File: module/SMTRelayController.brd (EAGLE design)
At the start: 57.1 x 63.2 mm, 34 parts, among them Q1 2n3904, Q2 2n3904, Q3 2n3904, U1 L298

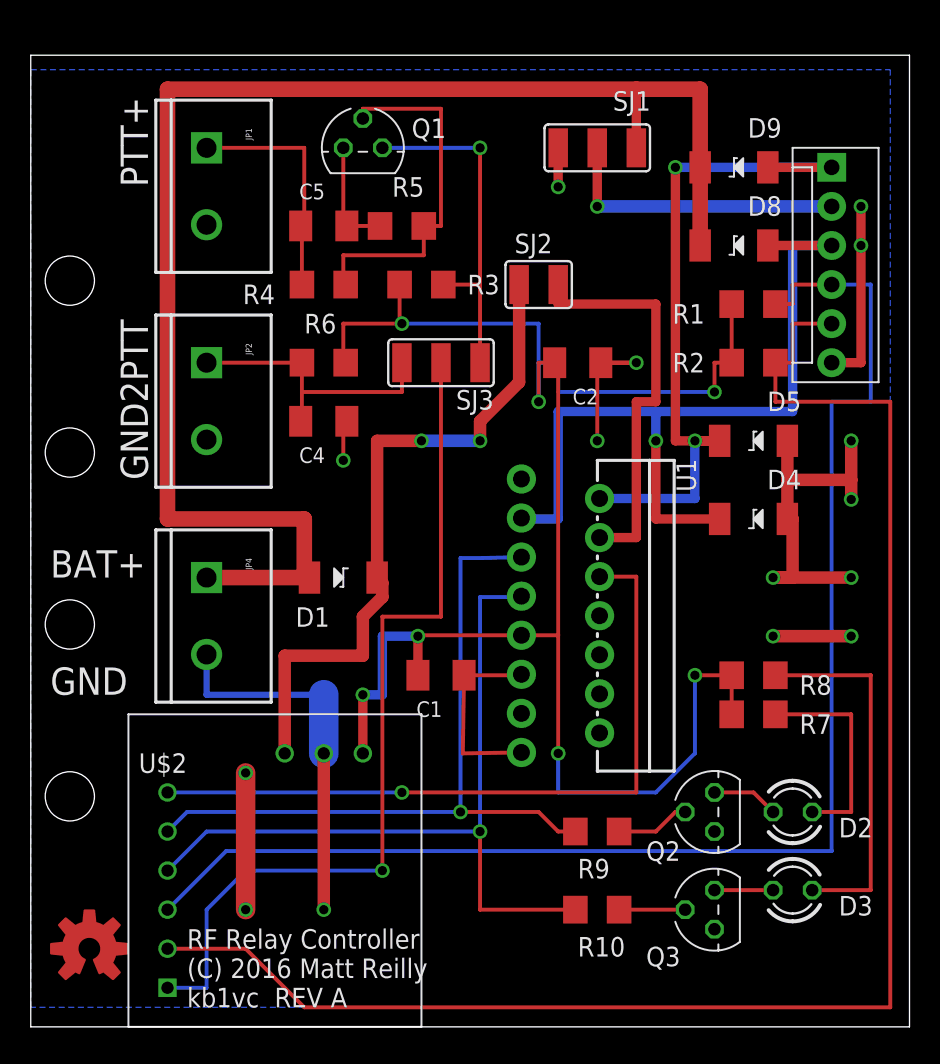
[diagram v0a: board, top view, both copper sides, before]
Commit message: Updates with OSHW logo, surface mount parts, and improved PTT2GND (protected) circuit.
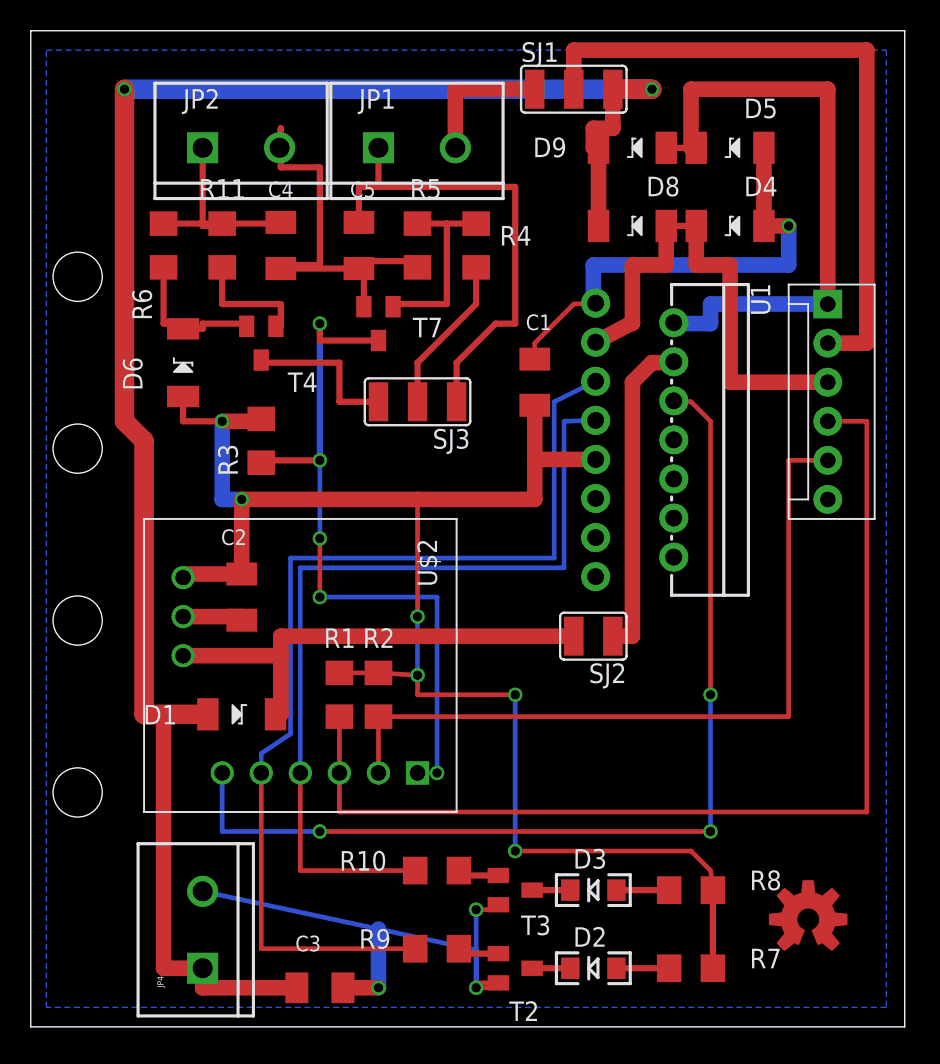
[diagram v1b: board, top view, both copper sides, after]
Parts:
- removed Q1, Q2, Q3: 2n3904, transistor:TO92
- added C3: 0.15, resistor:C1206K
- added D6: PMEG3030EP, kb1vc_robot_parts:SOD128
- added R11: 10K, rcl:R1206
- added T2, T3, T7: MMBT3904, transistor-neu-to92:SOT23-BEC
- added T4: MMBT3906, transistor-neu-to92:SOT23-BEC
- D2, D3: device led:LED3MM -> SparkFun-LED:LED-1206
- moved LOGO1 46.8 mm to (50.5, 6.99)
- moved R1 37.0 mm to (20.1, 21.6), turned to 90 degrees
- moved R2 32.6 mm to (22.6, 21.6), turned to 90 degrees
- moved C2 26.6 mm to (13.7, 27.9), turned to 270 degrees
- moved JP4 25.4 mm to (11.2, 3.81), turned to 90 degrees
- moved SJ2 23.1 mm to (36.6, 25.4)
- moved C1 20.0 mm to (32.8, 41.9), turned to 90 degrees
- moved D4 19.1 mm to (45.5, 52.1)
- moved D5 19.1 mm to (45.5, 57.1)
- moved R7 17.0 mm to (42.9, 3.81), turned to 0 degrees
- moved D2 16.5 mm to (36.6, 3.81)
- moved R3 14.5 mm to (15.0, 38.1), turned to 90 degrees
- moved R8 14.5 mm to (42.9, 8.89), turned to 0 degrees
- moved U$2 14.4 mm to (18.8, 22.9), turned to 270 degrees
- moved JP2 14.0 mm to (11.2, 57.1), turned to 0 degrees
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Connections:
- new net N$11: C4.1, JP2.1, R11.1, R6.1
- new net N$12: D6.P$2, R6.2, T4.E
- new net N$13: SJ3.3, T4.C
- net GND: now also C3.2, T2.E, T3.E, T7.E; no longer Q1.3, Q2.3, Q3.3
- net N$1: now also SJ3.1; no longer R4.2
- net N$10: now also T3.B; no longer Q3.2
- net N$2: now also R4.2, SJ3.2; no longer Q1.1, R3.1, SJ3.1
- net N$4: now also T7.B; no longer Q1.2
- net N$5: now also R11.2, T4.B; no longer C4.1, JP2.1, R6.1, SJ3.3
- net N$7: now also D2.C, T2.C; no longer D2.K, Q2.1
- net N$8: now also D3.C, T3.C; no longer D3.K, Q3.1
- net N$9: now also T2.B; no longer Q2.2
- net PTT_L: now also R3.1, T7.C; no longer SJ3.2
- net VCC: now also D6.P$1; no longer R6.2
- net V_RAW: now also C3.1
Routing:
- net RX_SENSE_IN: track 104.1 -> 49.5 mm
- net V_RAW: track 96.3 -> 122.0 mm, vias 0 -> 2
- net COM_COIL: track 19.0 -> 43.2 mm, vias 1 -> 0
- net TX_SENSE_IN: track 91.6 -> 68.4 mm
- net RX_COIL: track 53.3 -> 31.9 mm, vias 1 -> 0
- net N$3: track 24.0 -> 3.43 mm
- net TX_CTL: track 48.0 -> 66.7 mm, vias 1 -> 0
- net RELAY_ENA: track 46.9 -> 65.2 mm, vias 1 -> 3
- net N$1: track 15.5 -> 31.3 mm
- net VCC: track 120.3 -> 105.1 mm, vias 7 -> 6
- net N$11: track 0.00 -> 14.2 mm
- net V_IN: track 44.0 -> 30.8 mm, vias 2 -> 0
- net N$2: track 22.7 -> 10.3 mm, vias 1 -> 0
- net N$4: track 23.6 -> 12.7 mm
- net N$5: track 18.5 -> 7.96 mm
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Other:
- board size 57.1 x 63.2 mm -> 56.8 x 64.8 mm
- board text added: "+V"
- board text added: "PTT2GND"
- board text added: "PTT2PLUS"
- board text removed: "BAT+"
- board text removed: "GND2PTT"
- board text removed: "PTT+"
- board text removed: "RF Relay Controller (C) 2016 Matt Reilly kb1vc REV A"
